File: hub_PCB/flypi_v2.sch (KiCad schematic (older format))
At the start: 28 parts, among them CON1 BARREL_JACK, J12 USB_A, P1 D1, P10 A2, P11 A3, P12 I2C 1, P13 I2C 2, P14 12V, P15 UART, P2 D2, P3 D3, P4 D4, P5 D5, P6 D6, P7 D7, P8 D8, P9 A1, U1 LM2596, U2 LM2596, U3 ESP32-DEVKITC-32D

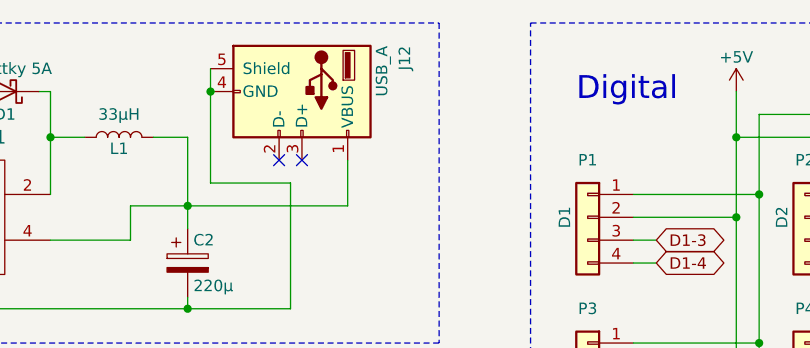
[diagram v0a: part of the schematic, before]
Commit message: Update flypi_v2.sch
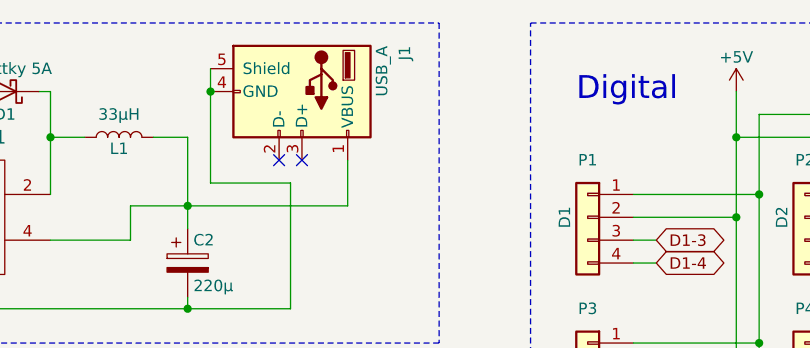
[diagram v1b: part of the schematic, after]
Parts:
- renumbered J12 to J1
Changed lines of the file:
@@
 $EndComp
 $Comp
-L Connector:USB_A J12
+L Connector:USB_A J1
 U 1 1 59ED406F
 P 4600 1750
-F 0 "J12" H 4400 2200 50  0000 L CNN
+F 0 "J1" H 4400 2200 50  0000 L CNN
 F 1 "USB_A" H 4400 2100 50  0000 L CNN
 F 2 "Connector_USB:USB_A_Vertical" H 4750 1700 50  0001 C CNN

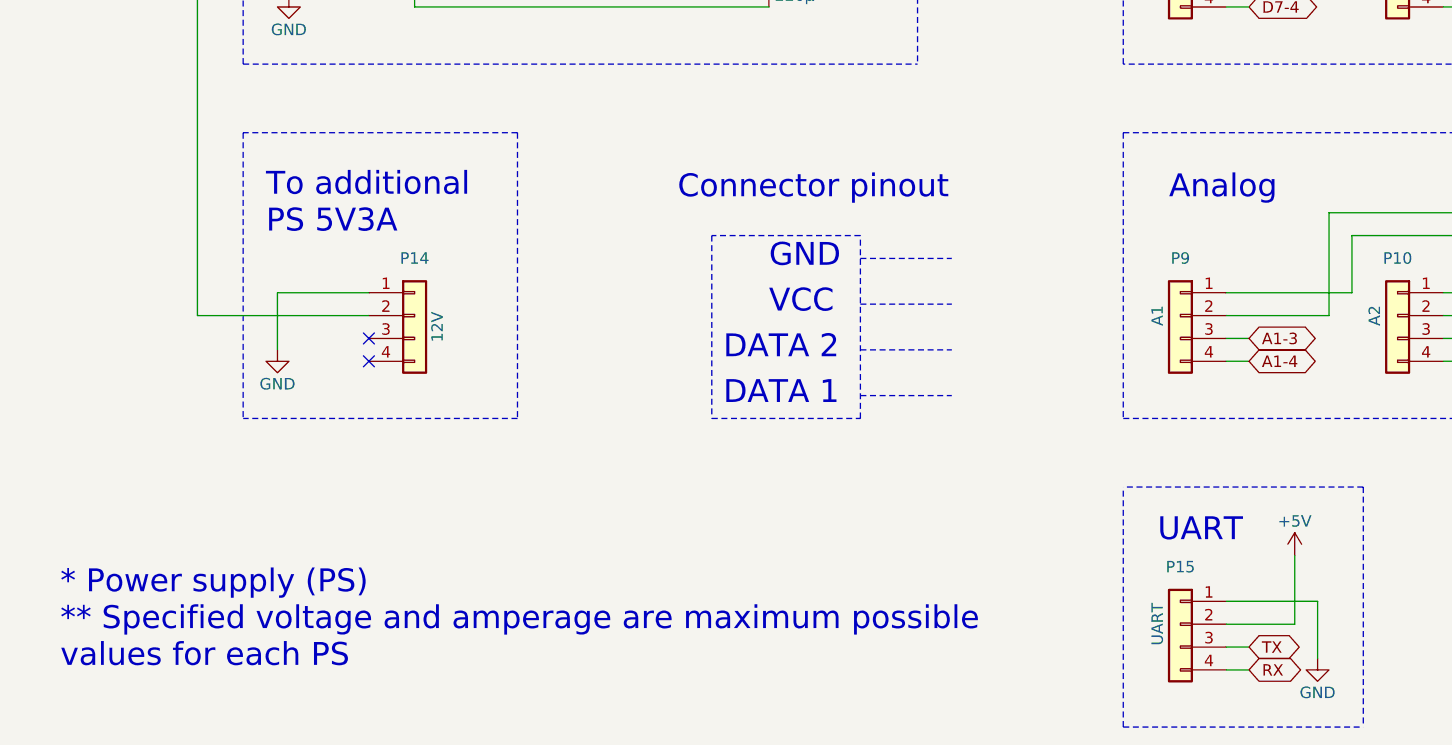
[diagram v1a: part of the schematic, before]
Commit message: Added more information regarding connector pinout
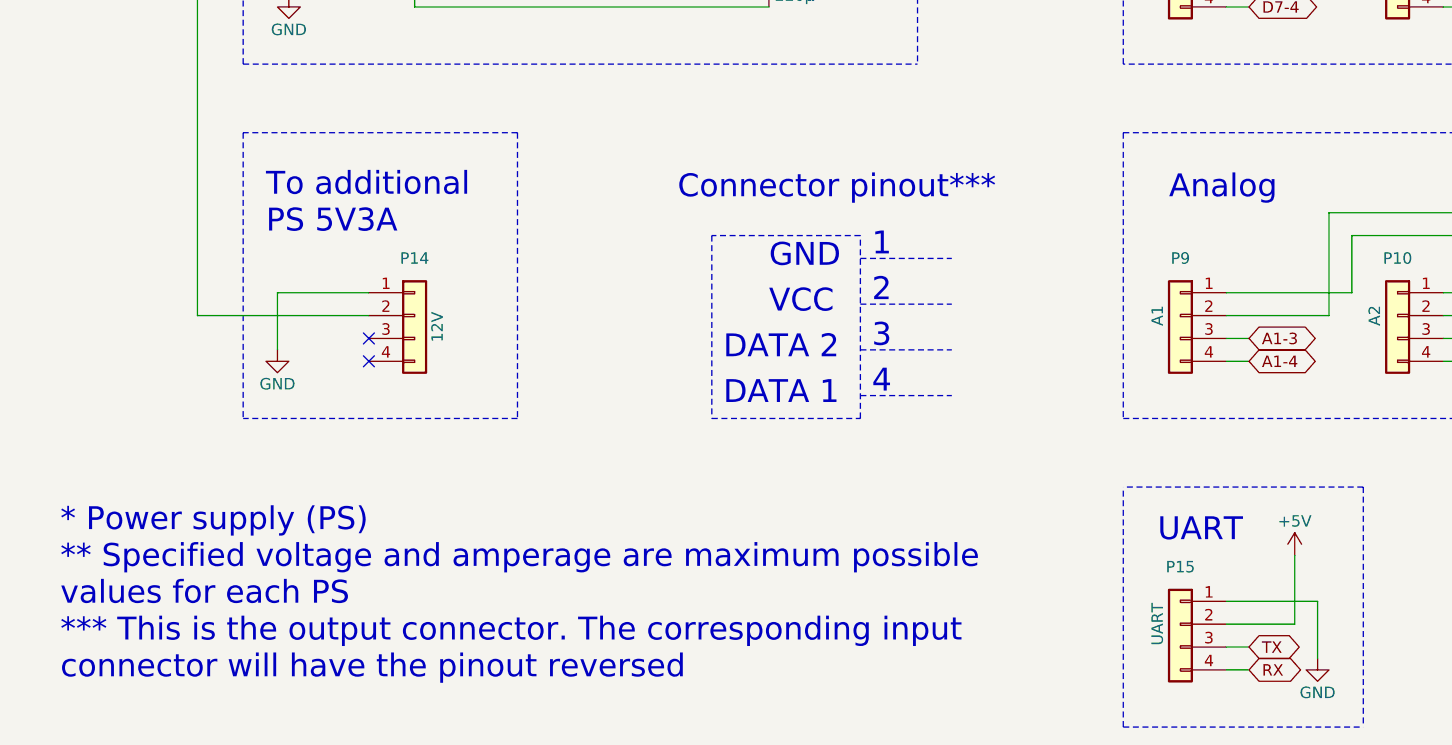
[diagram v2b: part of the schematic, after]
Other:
- note added: "* Power supply (PS)\n** Specified voltage and amperage are maximum possible\nvalues for each PS \n*** This is the output connector. The corresponding input\nconnector will have the pinout reversed"
- note added: "1"
- note added: "2"
- note added: "3"
- note added: "4"
- note added: "Connector pinout***"
- note removed: "* Power supply (PS)\n** Specified voltage and amperage are maximum possible\nvalues for each PS"
- note removed: "Connector pinout"
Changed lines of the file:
@@
 	2950 6250 1750 6250
 Text Notes 3650 5300 0    100  ~ 0
-Connector pinout
+Connector pinout***
 Wire Notes Line
 	1750 5000 1750 6250
@@
 	-1   0    0    1
 $EndComp
-Text Notes 950  7350 0    100  ~ 0
-* Power supply (PS)\n** Specified voltage and amperage are maximum possible\nvalues for each PS
 Wire Wire Line
 	3450 3450 3500 3450
@@
 	-1   0    0    -1
 $EndComp
+Text Notes 950  7400 0    100  ~ 0
+* Power supply (PS)\n** Specified voltage and amperage are maximum possible\nvalues for each PS \n*** This is the output connector. The corresponding input\nconnector will have the pinout reversed
+Text Notes 4500 5550 0    100  ~ 0
+1
+Text Notes 4500 5750 0    100  ~ 0
+2
+Text Notes 4500 5950 0    100  ~ 0
+3
+Text Notes 4500 6150 0    100  ~ 0
+4
 $EndSCHEMATC

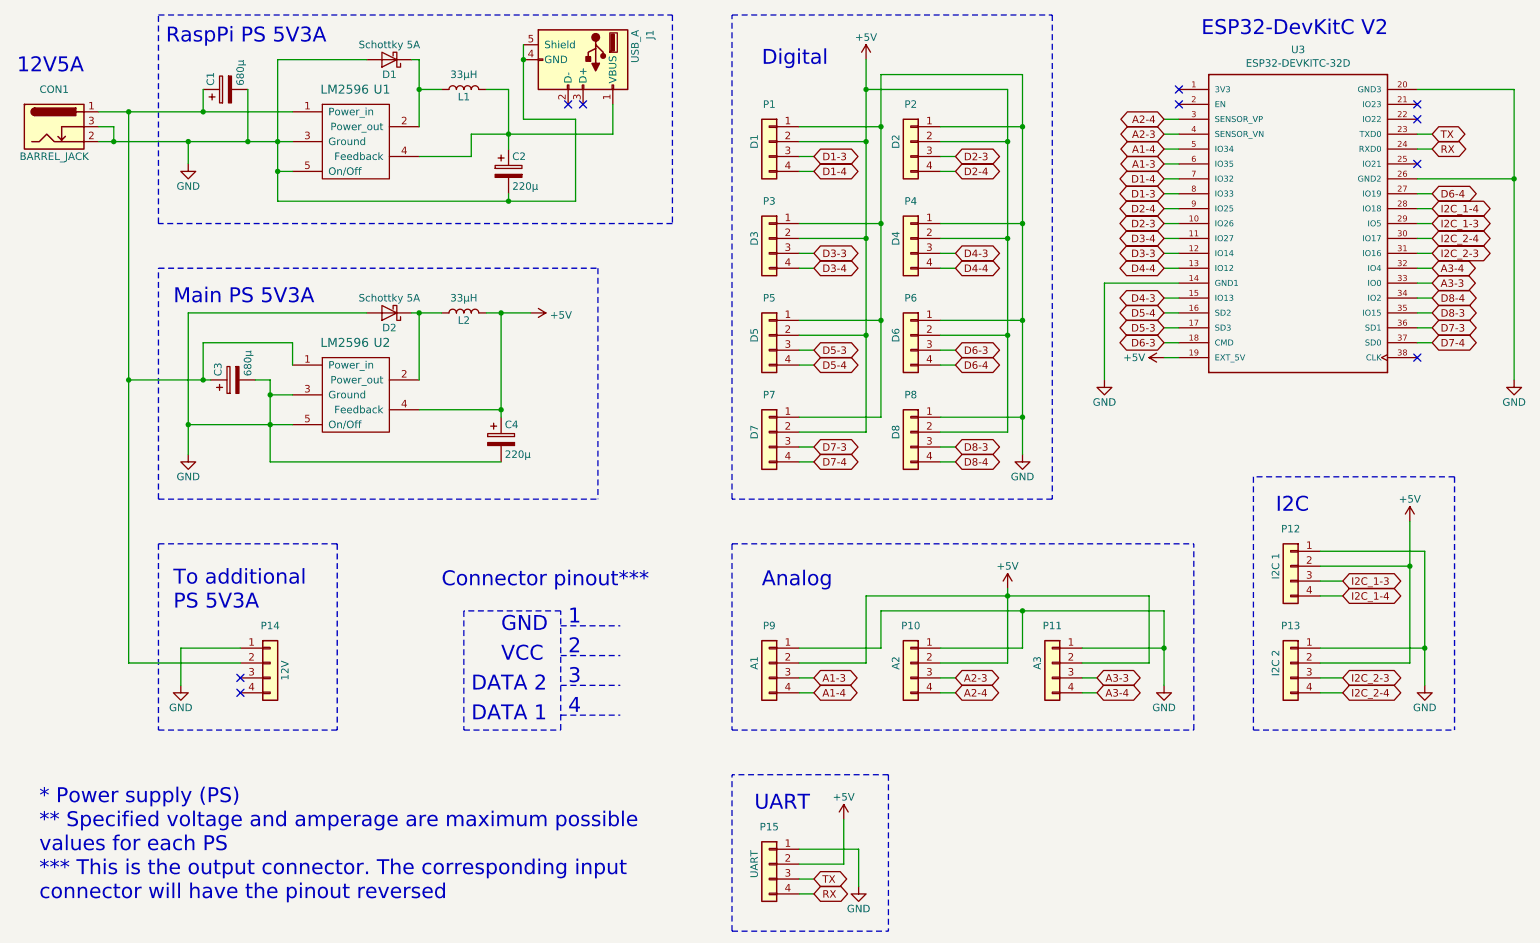
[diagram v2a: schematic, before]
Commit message: Changed pinout to VCC-GND
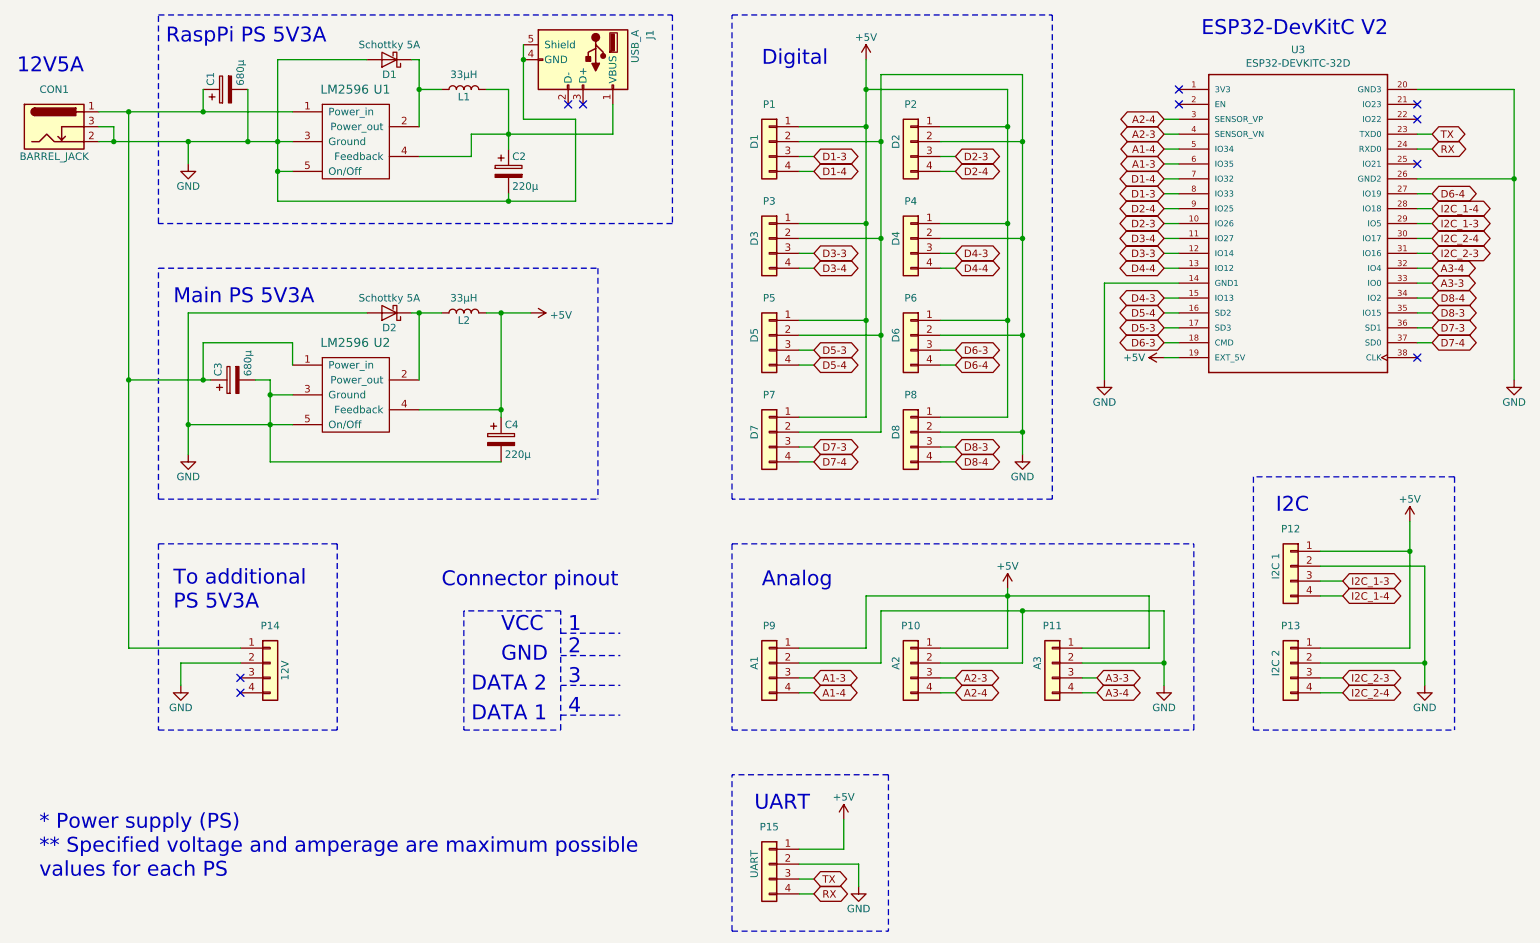
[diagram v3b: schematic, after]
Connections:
- net +5V: now also P1.1 (Pin_1), P10.1 (Pin_1), P11.1 (Pin_1), P12.1 (Pin_1), P13.1 (Pin_1), P15.1 (Pin_1), P2.1 (Pin_1), P3.1 (Pin_1), P4.1 (Pin_1), P5.1 (Pin_1), P6.1 (Pin_1), P7.1 (Pin_1), P8.1 (Pin_1), P9.1 (Pin_1); no longer P1.2 (Pin_2), P10.2 (Pin_2), P11.2 (Pin_2), P12.2 (Pin_2), P13.2 (Pin_2), P15.2 (Pin_2), P2.2 (Pin_2), P3.2 (Pin_2), P4.2 (Pin_2), P5.2 (Pin_2), P6.2 (Pin_2), P7.2 (Pin_2), P8.2 (Pin_2), P9.2 (Pin_2)
- net GND: now also P1.2 (Pin_2), P10.2 (Pin_2), P11.2 (Pin_2), P12.2 (Pin_2), P13.2 (Pin_2), P14.2 (Pin_2), P15.2 (Pin_2), P2.2 (Pin_2), P3.2 (Pin_2), P4.2 (Pin_2), P5.2 (Pin_2), P6.2 (Pin_2), P7.2 (Pin_2), P8.2 (Pin_2), P9.2 (Pin_2); no longer P1.1 (Pin_1), P10.1 (Pin_1), P11.1 (Pin_1), P12.1 (Pin_1), P13.1 (Pin_1), P14.1 (Pin_1), P15.1 (Pin_1), P2.1 (Pin_1), P3.1 (Pin_1), P4.1 (Pin_1), P5.1 (Pin_1), P6.1 (Pin_1), P7.1 (Pin_1), P8.1 (Pin_1), P9.1 (Pin_1)
- net at C1.1, C3.1, CON1.1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: now also P14.1 (Pin_1); no longer P14.2 (Pin_2)
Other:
- note added: "* Power supply (PS)\n** Specified voltage and amperage are maximum possible\nvalues for each PS"
- note added: "Connector pinout"
- note removed: "* Power supply (PS)\n** Specified voltage and amperage are maximum possible\nvalues for each PS \n*** This is the output connector. The corresponding input\nconnector will have the pinout reversed"
- note removed: "Connector pinout***"
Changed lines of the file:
@@
 	2650 3650 2650 3800
 Wire Wire Line
-	6600 2200 6050 2200
-Connection ~ 6600 2200
-Wire Wire Line
-	6600 3500 6050 3500
-Wire Wire Line
 	1950 3450 1950 4200
 Wire Wire Line
-	6500 2300 6050 2300
-Wire Wire Line
 	6500 1950 7450 1950
-Wire Wire Line
-	6500 3600 6050 3600
-Wire Wire Line
-	6500 4250 6050 4250
 $Comp
 L ESP32-DEVKITC-32D:ESP32-DEVKITC-32D U3
@@
 	4050 3450 4050 4100
 Connection ~ 4050 3450
-Wire Wire Line
-	6050 4150 6600 4150
-Connection ~ 6500 2300
-Wire Wire Line
-	7000 4250 7450 4250
-Wire Wire Line
-	7000 4150 7550 4150
-Wire Wire Line
-	7000 3600 7450 3600
-Wire Wire Line
-	7000 3500 7550 3500
-Wire Wire Line
-	7000 2300 7450 2300
-Connection ~ 7450 2300
-Wire Wire Line
-	7000 2200 7550 2200
-Connection ~ 7550 2200
 Connection ~ 6500 1950
 Wire Wire Line
 	6600 1850 7550 1850
-Wire Wire Line
-	9550 5800 10150 5800
-Wire Wire Line
-	10150 5150 9550 5150
-Wire Wire Line
-	9550 5700 10250 5700
-Wire Wire Line
-	10250 5050 9550 5050
-Connection ~ 10150 5150
-Connection ~ 10250 5700
 $Comp
 L power:+5V #PWR0105
@@
 $EndComp
 Wire Wire Line
-	7550 1850 7550 2200
-Wire Wire Line
-	7450 1950 7450 2300
-Wire Wire Line
-	6600 1850 6600 2200
-Wire Wire Line
-	6500 1950 6500 2300
-Wire Wire Line
-	7550 2200 7550 2850
-Wire Wire Line
-	7450 2300 7450 2950
-Wire Wire Line
-	7000 2850 7550 2850
-Wire Wire Line
-	7000 2950 7450 2950
-Wire Wire Line
-	6500 2300 6500 2950
-Wire Wire Line
 	7100 3150 7000 3150
 Wire Wire Line
@@
 Text GLabel 6150 3050 2    50   BiDi ~ 0
 D3-3
-Wire Wire Line
-	6500 2950 6050 2950
-Wire Wire Line
-	6600 2850 6050 2850
-Wire Wire Line
-	6600 2200 6600 2850
 $Comp
 L Connector_Generic:Conn_01x04 P4
@@
 	-1   0    0    -1
 $EndComp
-Connection ~ 6500 2950
-Connection ~ 6600 2850
-Wire Wire Line
-	6500 2950 6500 3600
-Wire Wire Line
-	6600 2850 6600 3500
-Connection ~ 7450 2950
-Connection ~ 7550 2850
-Wire Wire Line
-	7550 2850 7550 3500
-Wire Wire Line
-	7450 2950 7450 3600
-Connection ~ 6500 3600
-Connection ~ 6600 3500
-Wire Wire Line
-	6500 3600 6500 4250
-Wire Wire Line
-	6600 3500 6600 4150
-Connection ~ 7450 3600
-Connection ~ 7550 3500
-Wire Wire Line
-	7450 3600 7450 4250
-Wire Wire Line
-	7550 3500 7550 4150
-Connection ~ 7550 4150
-Wire Wire Line
-	7550 4150 7550 4400
 Wire Wire Line
 	7450 5350 8400 5350
@@
 Wire Notes Line
 	5600 6250 8700 6250
-Wire Wire Line
-	10150 5800 10150 5150
-Wire Wire Line
-	10250 5700 10250 5050
-Wire Wire Line
-	10250 5700 10250 5950
 Wire Notes Line
 	9100 6250 10450 6250
@@
 Wire Notes Line
 	10450 4550 10450 6250
-Wire Wire Line
-	10150 4850 10150 5150
 Text Notes 1850 3400 0    100  ~ 0
 Main PS 5V3A
@@
 Text GLabel 10300 2250 2    50   BiDi ~ 0
 TX
-Wire Wire Line
-	6050 7150 6350 7150
-Wire Wire Line
-	6350 6850 6350 7150
-Wire Wire Line
-	6050 7050 6450 7050
-Wire Wire Line
-	6450 7050 6450 7300
 $Comp
 L power:+5V #PWR0114
@@
 Wire Wire Line
 	10200 2350 10300 2350
-Wire Wire Line
-	1900 5700 2300 5700
 $Comp
 L Connector_Generic:Conn_01x04 P14
@@
 Text Notes 1850 5450 0    100  ~ 0
 To additional\nPS 5V3A
-Wire Wire Line
-	1900 5700 1900 5950
 Text Notes 800  1850 0    100  ~ 0
 12V5A
-Wire Wire Line
-	1550 5800 2300 5800
 NoConn ~ 2300 5900
 NoConn ~ 2300 6000
@@
 	2950 6250 1750 6250
 Text Notes 3650 5300 0    100  ~ 0
-Connector pinout***
+Connector pinout
 Wire Notes Line
 	1750 5000 1750 6250
@@
 	4450 5950 4850 5950
 Wire Notes Line style solid rgb(255, 0, 0)
-	4450 5750 4850 5750
+	4450 5600 4850 5600
 Text Notes 3850 6200 0    100  ~ 0
 DATA 1
 Text Notes 3850 6000 0    100  ~ 0
 DATA 2
-Text Notes 4050 5800 0    100  ~ 0
+Text Notes 4050 5600 0    100  ~ 0
 VCC
 Wire Wire Line
@@
 Connection ~ 1550 3900
 Wire Wire Line
-	1550 3900 1550 5800
+	1550 3900 1550 5700
 Wire Wire Line
 	1550 2100 1550 3900
@@
 	1750 2850 1750 1450
 Wire Wire Line
-	8500 5450 8500 5700
-Wire Wire Line
 	6600 5450 7550 5450
-Wire Wire Line
-	6050 5700 6600 5700
-Wire Wire Line
-	6600 5700 6600 5450
-Wire Wire Line
-	7550 5700 7550 5450
-Wire Wire Line
-	7000 5700 7550 5700
 Connection ~ 7550 5450
 Wire Wire Line
 	7550 5450 8500 5450
-Wire Wire Line
-	7000 5800 7450 5800
-Wire Wire Line
-	7450 5800 7450 5350
-Wire Wire Line
-	6050 5800 6500 5800
-Wire Wire Line
-	6500 5800 6500 5350
-Wire Wire Line
-	7950 5700 8500 5700
-Connection ~ 8500 5700
-Wire Wire Line
-	8500 5700 8500 5950
-Wire Wire Line
-	7950 5800 8400 5800
-Wire Wire Line
-	8400 5800 8400 5350
 Wire Notes Line
 	1750 3150 4700 3150
@@
 	10200 2650 10300 2650
 Wire Notes Line style solid rgb(0, 0, 0)
-	4450 5550 4850 5550
+	4450 5750 4850 5750
 Wire Notes Line style solid
 	4450 6250 4450 5450
-Text Notes 4050 5600 0    100  ~ 0
+Text Notes 4050 5800 0    100  ~ 0
 GND
 $Comp
@@
 	-1   0    0    -1
 $EndComp
-Text Notes 950  7400 0    100  ~ 0
-* Power supply (PS)\n** Specified voltage and amperage are maximum possible\nvalues for each PS \n*** This is the output connector. The corresponding input\nconnector will have the pinout reversed
-Text Notes 4500 5550 0    100  ~ 0
+Text Notes 950  7250 0    100  ~ 0
+* Power supply (PS)\n** Specified voltage and amperage are maximum possible\nvalues for each PS
+Text Notes 4500 5600 0    100  ~ 0
 1
 Text Notes 4500 5750 0    100  ~ 0
@@
 Text Notes 4500 6150 0    100  ~ 0
 4
+Wire Wire Line
+	6050 3500 6500 3500
+Connection ~ 6500 3500
+Wire Wire Line
+	6500 3500 6500 4150
+Wire Wire Line
+	6050 3600 6600 3600
+Connection ~ 6600 3600
+Wire Wire Line
+	6050 2950 6600 2950
+Connection ~ 6600 2950
+Wire Wire Line
+	6600 2950 6600 3600
+Wire Wire Line
+	6050 2850 6500 2850
+Connection ~ 6500 2850
+Wire Wire Line
+	6500 2850 6500 3500
+Wire Wire Line
+	6500 1950 6500 2200
+Wire Wire Line
+	6600 1850 6600 2300
+Wire Wire Line
+	6050 2300 6600 2300
+Connection ~ 6600 2300
+Wire Wire Line
+	6600 2300 6600 2950
+Wire Wire Line
+	6050 2200 6500 2200
+Connection ~ 6500 2200
+Wire Wire Line
+	6500 2200 6500 2850
+Wire Wire Line
+	6050 4150 6500 4150
+Wire Wire Line
+	6050 4250 6600 4250
+Wire Wire Line
+	6600 3600 6600 4250
+Wire Wire Line
+	7000 4150 7450 4150
+Wire Wire Line
+	7000 4250 7550 4250
+Connection ~ 7550 4250
+Wire Wire Line
+	7550 4250 7550 4400
+Wire Wire Line
+	7000 3600 7550 3600
+Connection ~ 7550 3600
+Wire Wire Line
+	7550 3600 7550 4250
+Wire Wire Line
+	7000 3500 7450 3500
+Connection ~ 7450 3500
+Wire Wire Line
+	7450 3500 7450 4150
+Wire Wire Line
+	7000 2950 7550 2950
+Connection ~ 7550 2950
+Wire Wire Line
+	7550 2950 7550 3600
+Wire Wire Line
+	7000 2850 7450 2850
+Connection ~ 7450 2850
+Wire Wire Line
+	7450 2850 7450 3500
+Wire Wire Line
+	7450 1950 7450 2200
+Wire Wire Line
+	7550 1850 7550 2300
+Wire Wire Line
+	7000 2300 7550 2300
+Connection ~ 7550 2300
+Wire Wire Line
+	7550 2300 7550 2950
+Wire Wire Line
+	7000 2200 7450 2200
+Connection ~ 7450 2200
+Wire Wire Line
+	7450 2200 7450 2850
+Wire Wire Line
+	6050 7050 6350 7050
+Wire Wire Line
+	6350 7050 6350 6850
+Wire Wire Line
+	6050 7150 6450 7150
+Wire Wire Line
+	6450 7150 6450 7300
+Wire Wire Line
+	6050 5700 6500 5700
+Wire Wire Line
+	6500 5700 6500 5350
+Wire Wire Line
+	6050 5800 6600 5800
+Wire Wire Line
+	6600 5450 6600 5800
+Wire Wire Line
+	7000 5700 7450 5700
+Wire Wire Line
+	7450 5700 7450 5350
+Wire Wire Line
+	7000 5800 7550 5800
+Wire Wire Line
+	7550 5450 7550 5800
+Wire Wire Line
+	8500 5450 8500 5800
+Wire Wire Line
+	7950 5700 8400 5700
+Wire Wire Line
+	8400 5700 8400 5350
+Wire Wire Line
+	7950 5800 8500 5800
+Connection ~ 8500 5800
+Wire Wire Line
+	8500 5800 8500 5950
+Wire Wire Line
+	10150 4850 10150 5050
+Wire Wire Line
+	9550 5050 10150 5050
+Connection ~ 10150 5050
+Wire Wire Line
+	10150 5050 10150 5700
+Wire Wire Line
+	9550 5150 10250 5150
+Wire Wire Line
+	10250 5150 10250 5800
+Wire Wire Line
+	9550 5700 10150 5700
+Wire Wire Line
+	9550 5800 10250 5800
+Connection ~ 10250 5800
+Wire Wire Line
+	10250 5800 10250 5950
+Wire Wire Line
+	2300 5800 1900 5800
+Wire Wire Line
+	1900 5800 1900 5950
+Wire Wire Line
+	2300 5700 1550 5700
 $EndSCHEMATC
